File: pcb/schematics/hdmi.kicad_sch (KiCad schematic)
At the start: 22 parts

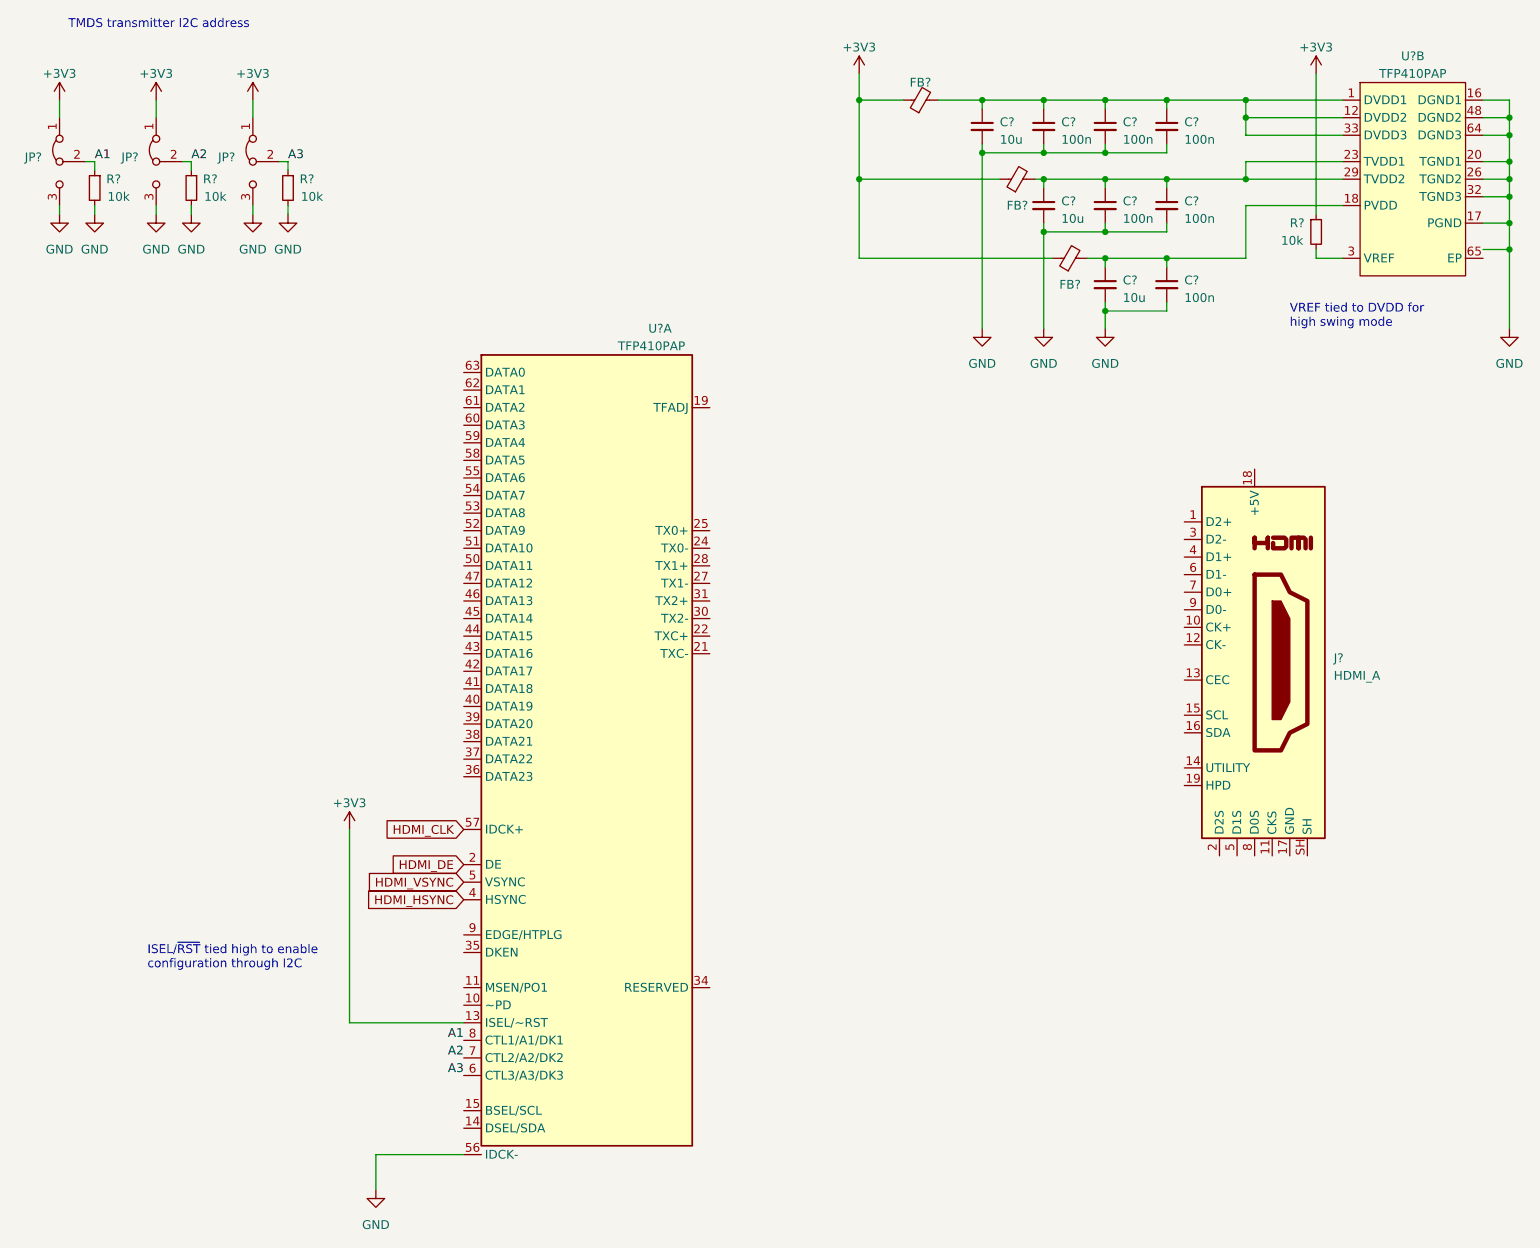
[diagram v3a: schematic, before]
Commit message: add hdmi frontend
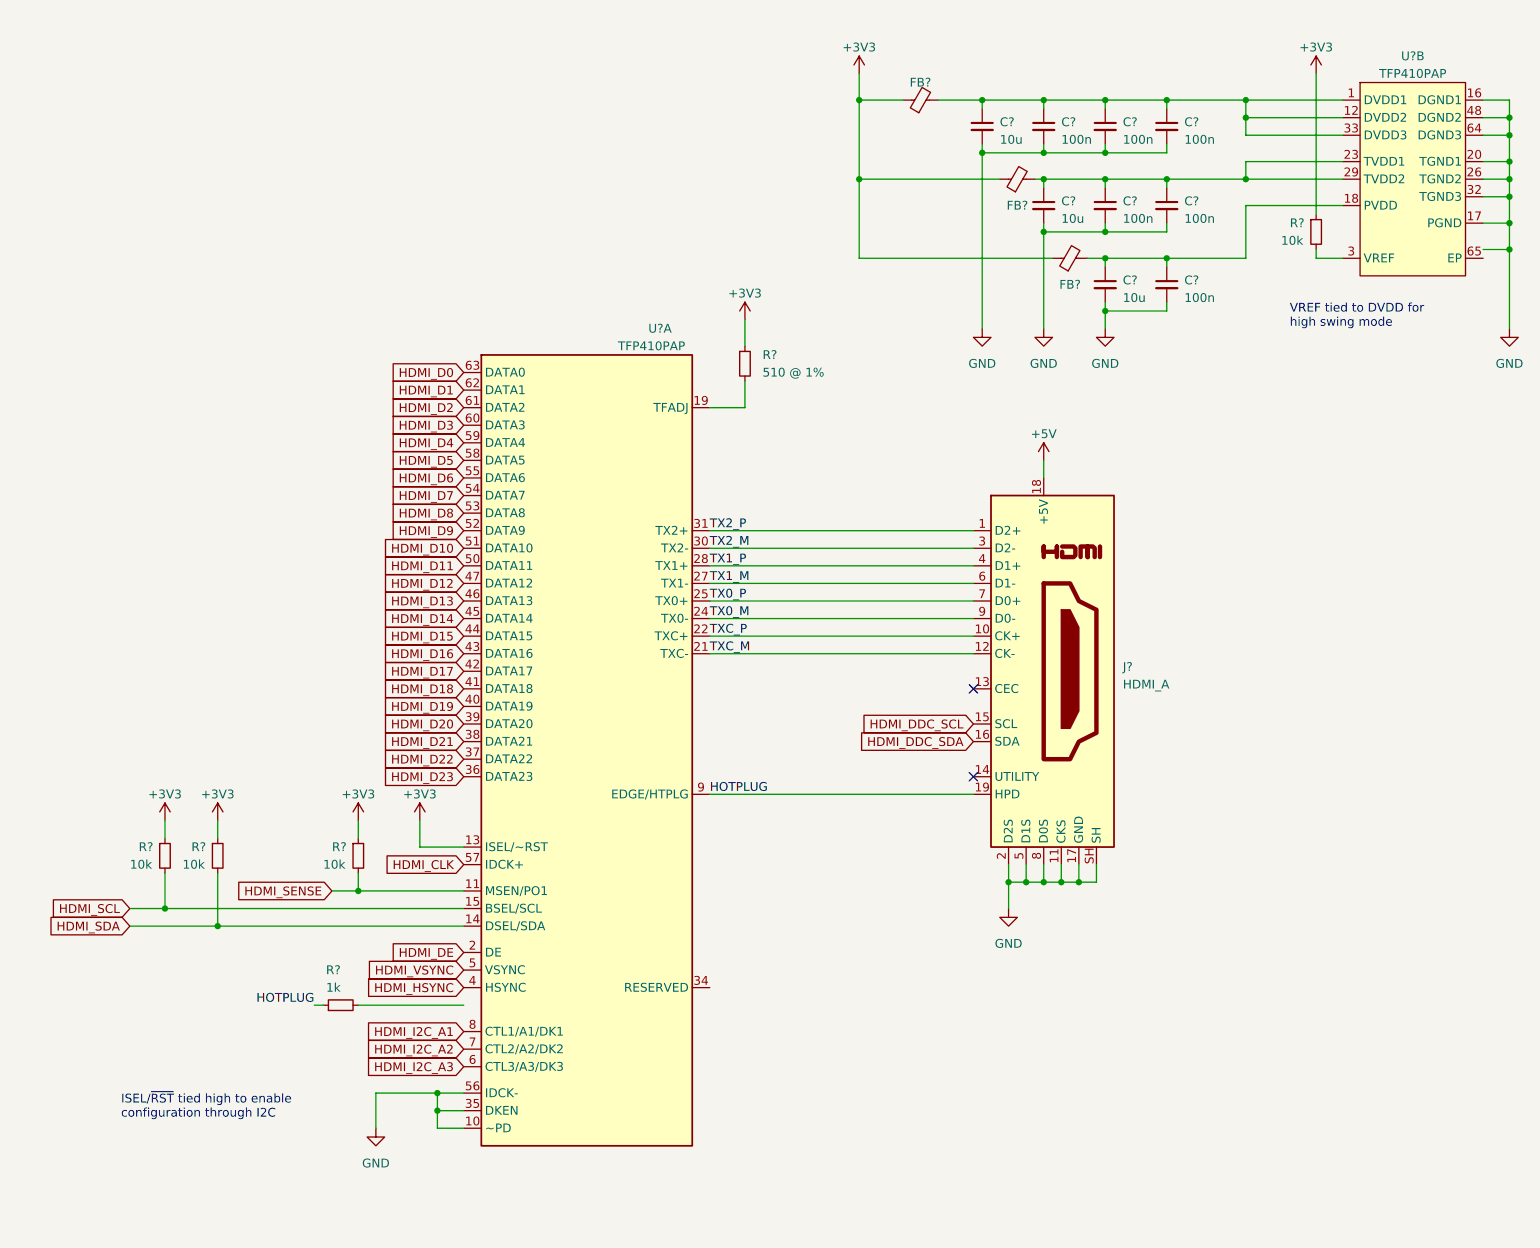
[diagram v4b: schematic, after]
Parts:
- removed JP? (x3): Jumper_3_Bridged12, symbol Jumper:Jumper_3_Bridged12
- removed R? (x3): 10k, symbol Device:R_Small
- added R? (x3): 10k, symbol Device:R_Small
- added R?: 1k, symbol Device:R_Small
- added R?: 510 @ 1%, symbol Device:R_Small
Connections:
- net +3V3: now also R?.1, R?.1, R?.1, R?.1
- net GND: now also J?.11 (CKS), J?.17 (GND), J?.2 (D2S), J?.5 (D1S), J?.8 (D0S), J?.SH, U?.10 (~PD), U?.35 (DKEN)
- net TX2_P: now reaches J?.1 (D2+)
- net TX2_P: now also U?.31 (TX2+)
- net TXC_P: now reaches J?.10 (CK+)
- net TXC_P: now also U?.22 (TXC+)
- net TXC_M: now reaches J?.12 (CK-)
- net TXC_M: now also U?.21 (TXC-)
- net HDMI_DDC_SCL: now reaches J?.15 (SCL)
- net HDMI_DDC_SDA: now reaches J?.16 (SDA)
- net +5V: now reaches J?.18 (+5V)
- net HOTPLUG: now reaches J?.19 (HPD)
- net HOTPLUG: now also U?.9 (EDGE/HTPLG), R?.1
- net TX2_M: now reaches J?.3 (D2-)
- net TX2_M: now also U?.30 (TX2-)
- net TX1_P: now reaches J?.4 (D1+)
- net TX1_P: now also U?.28 (TX1+)
- net TX1_M: now reaches J?.6 (D1-)
- net TX1_M: now also U?.27 (TX1-)
- net TX0_P: now reaches J?.7 (D0+)
- net TX0_P: now also U?.25 (TX0+)
- net TX0_M: now reaches J?.9 (D0-)
- net TX0_M: now also U?.24 (TX0-)
- net HDMI_SENSE: now reaches U?.11 (MSEN/PO1)
- net HDMI_SENSE: now also R?.2
- net HDMI_SDA: now reaches U?.14 (DSEL/SDA)
- net HDMI_SDA: now also R?.2
- net HDMI_SCL: now reaches U?.15 (BSEL/SCL)
- net HDMI_SCL: now also R?.2
- net at U?.19 (TFADJ): now also R?.2
- net HDMI_D23: now reaches U?.36 (DATA23)
- net HDMI_D22: now reaches U?.37 (DATA22)
- net HDMI_D21: now reaches U?.38 (DATA21)
- net HDMI_D20: now reaches U?.39 (DATA20)
- net HDMI_D19: now reaches U?.40 (DATA19)
- net HDMI_D18: now reaches U?.41 (DATA18)
- net HDMI_D17: now reaches U?.42 (DATA17)
- net HDMI_D16: now reaches U?.43 (DATA16)
- net HDMI_D15: now reaches U?.44 (DATA15)
- net HDMI_D14: now reaches U?.45 (DATA14)
- net HDMI_D13: now reaches U?.46 (DATA13)
- net HDMI_D12: now reaches U?.47 (DATA12)
- net HDMI_D11: now reaches U?.50 (DATA11)
- net HDMI_D10: now reaches U?.51 (DATA10)
- net HDMI_D9: now reaches U?.52 (DATA9)
- net HDMI_D8: now reaches U?.53 (DATA8)
- net HDMI_D7: now reaches U?.54 (DATA7)
- net HDMI_D6: now reaches U?.55 (DATA6)
- net HDMI_D5: now reaches U?.58 (DATA5)
- net HDMI_D4: now reaches U?.59 (DATA4)
- net HDMI_D3: now reaches U?.60 (DATA3)
- net HDMI_D2: now reaches U?.61 (DATA2)
- net HDMI_D1: now reaches U?.62 (DATA1)
- net HDMI_D0: now reaches U?.63 (DATA0)
- net A1 renamed HDMI_I2C_A1
- net A2 renamed HDMI_I2C_A2
- net A3 renamed HDMI_I2C_A3
- no-connect marks 0 -> 2
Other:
- note removed: "TMDS transmitter I2C address"
- moved on the sheet: J?, U?A

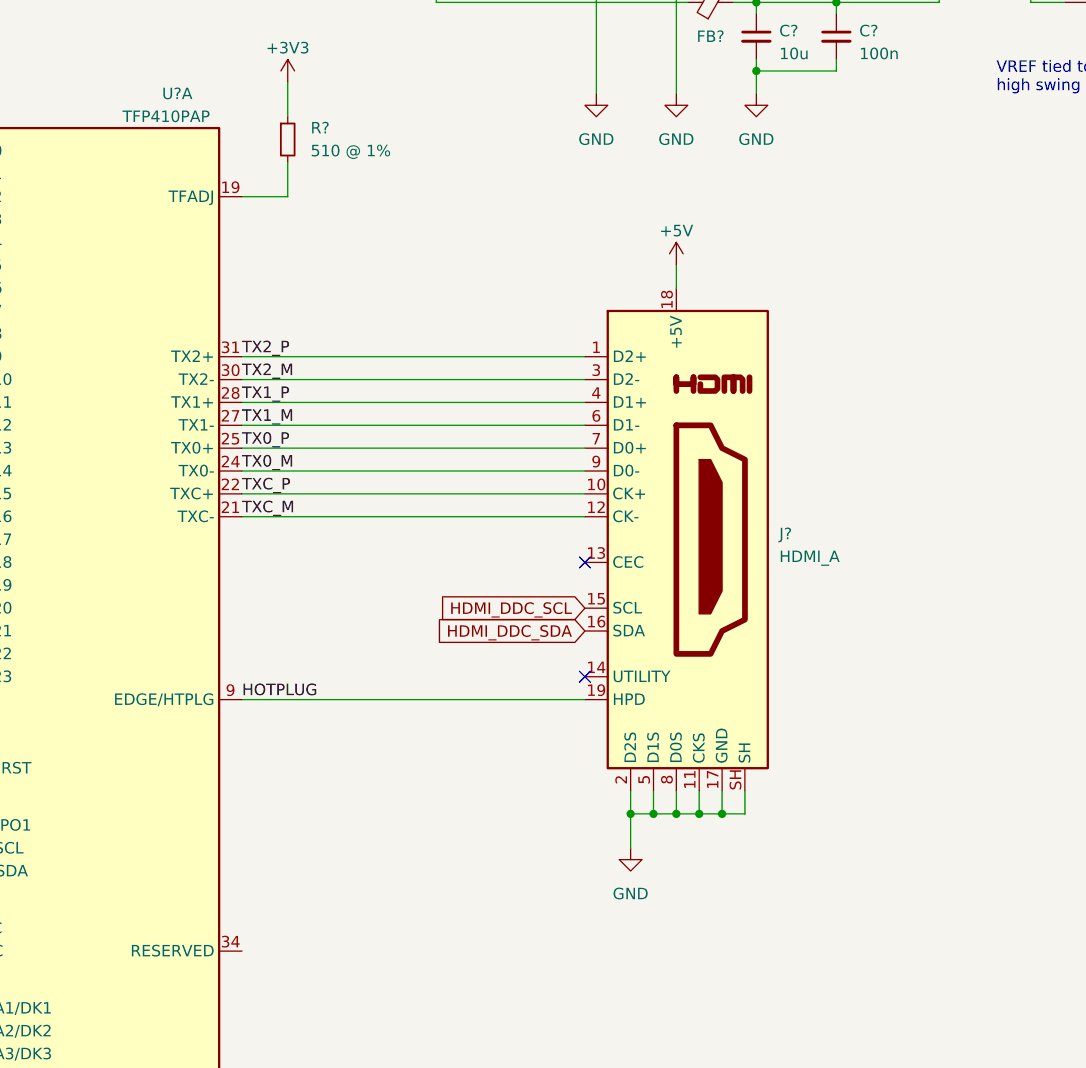
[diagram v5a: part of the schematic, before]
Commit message: add esd protection for the hdmi frontend
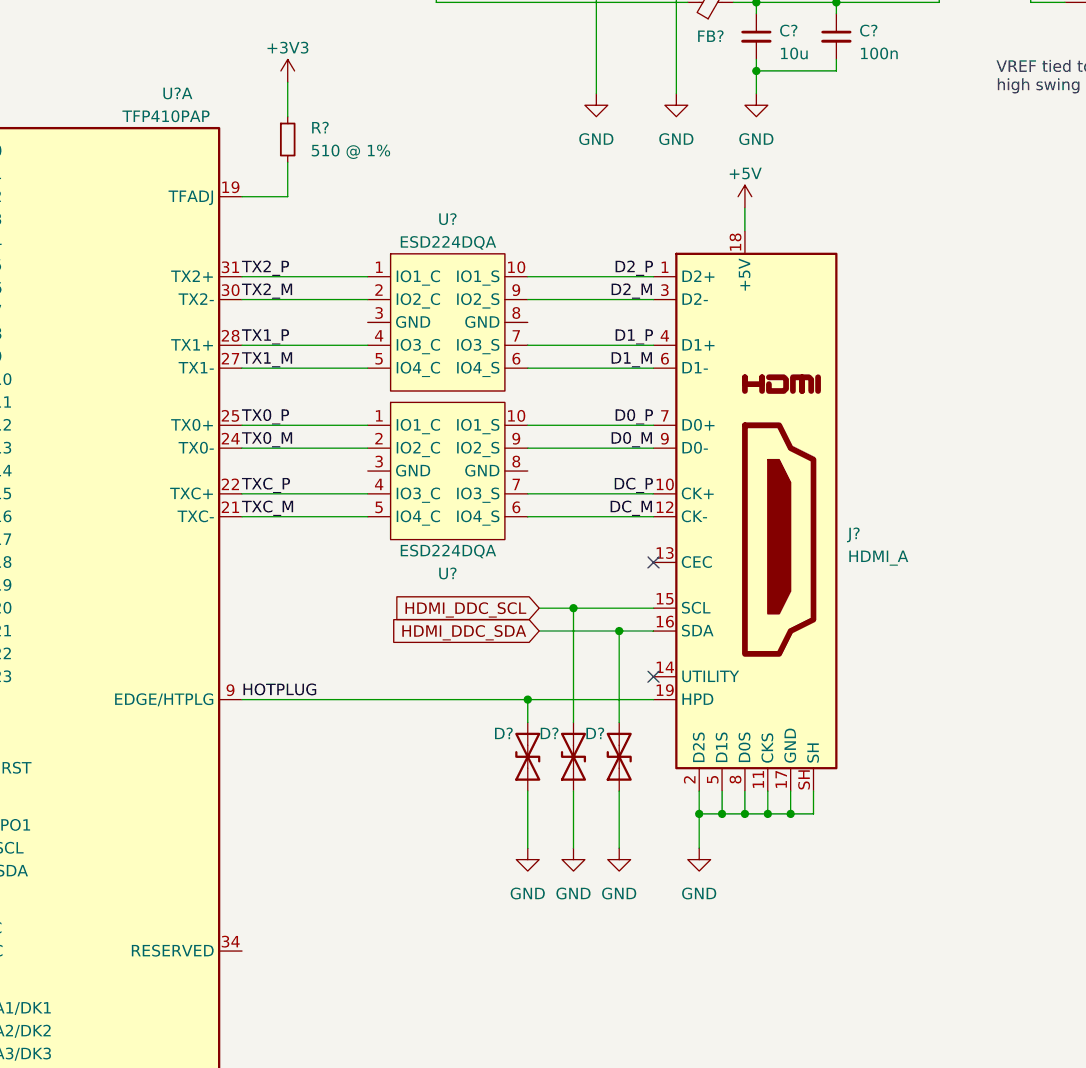
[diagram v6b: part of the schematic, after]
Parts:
- added D? (x3): D_TVS, symbol Device:D_TVS
- added U? (x2): ESD224DQA, symbol ESD224DQA:ESD224DQA
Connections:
- net GND: now also D?.1 (A1), D?.1 (A1), D?.1 (A1)
- net HDMI_DDC_SCL: now also D?.2 (A2)
- net HDMI_DDC_SDA: now also D?.2 (A2)
- net HOTPLUG: now also D?.2 (A2)
- net TX0_M: now also U?.2 (IO2_C); no longer J?.9 (D0-)
- net TX0_P: now also U?.1 (IO1_C); no longer J?.7 (D0+)
- net TX1_M: now also U?.5 (IO4_C); no longer J?.6 (D1-)
- net TX1_P: now also U?.4 (IO3_C); no longer J?.4 (D1+)
- net TX2_M: now also U?.2 (IO2_C); no longer J?.3 (D2-)
- net TX2_P: now also U?.1 (IO1_C); no longer J?.1 (D2+)
- net TXC_M: now also U?.5 (IO4_C); no longer J?.12 (CK-)
- net TXC_P: now also U?.4 (IO3_C); no longer J?.10 (CK+)
- new net D0_M: J?.9 (D0-), U?.9 (IO2_S)
- new net D0_P: J?.7 (D0+), U?.10 (IO1_S)
- new net D1_M: J?.6 (D1-), U?.6 (IO4_S)
- new net D1_P: J?.4 (D1+), U?.7 (IO3_S)
- new net D2_M: J?.3 (D2-), U?.9 (IO2_S)
- new net D2_P: J?.1 (D2+), U?.10 (IO1_S)
- new net DC_M: J?.12 (CK-), U?.6 (IO4_S)
- new net DC_P: J?.10 (CK+), U?.7 (IO3_S)
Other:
- moved on the sheet: J?

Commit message: moved i2c mux to another page
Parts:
- removed R? (x2): 10k, symbol Device:R_Small
- removed R?: 1k, symbol Device:R_Small
- added R?: 1k, symbol Device:R_Small
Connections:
- net GND: now also U?.3 (GND), U?.3 (GND), U?.8 (GND), U?.8 (GND)
- net HOTPLUG: now also R?.1; no longer D?.2 (A2), J?.19 (HPD)
- net HDMI_SCL renamed FPGA_SDA
- net HDMI_SDA renamed FPGA_SCL
- new net: D?.2 (A2), J?.19 (HPD), R?.2
